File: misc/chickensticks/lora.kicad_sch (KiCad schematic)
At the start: 30 parts, among them J8 S02-25200300, J9 SMA, U4 LR2021IMLTRT, Y2 TG2520SMN 32.0000M-MCGNNM0

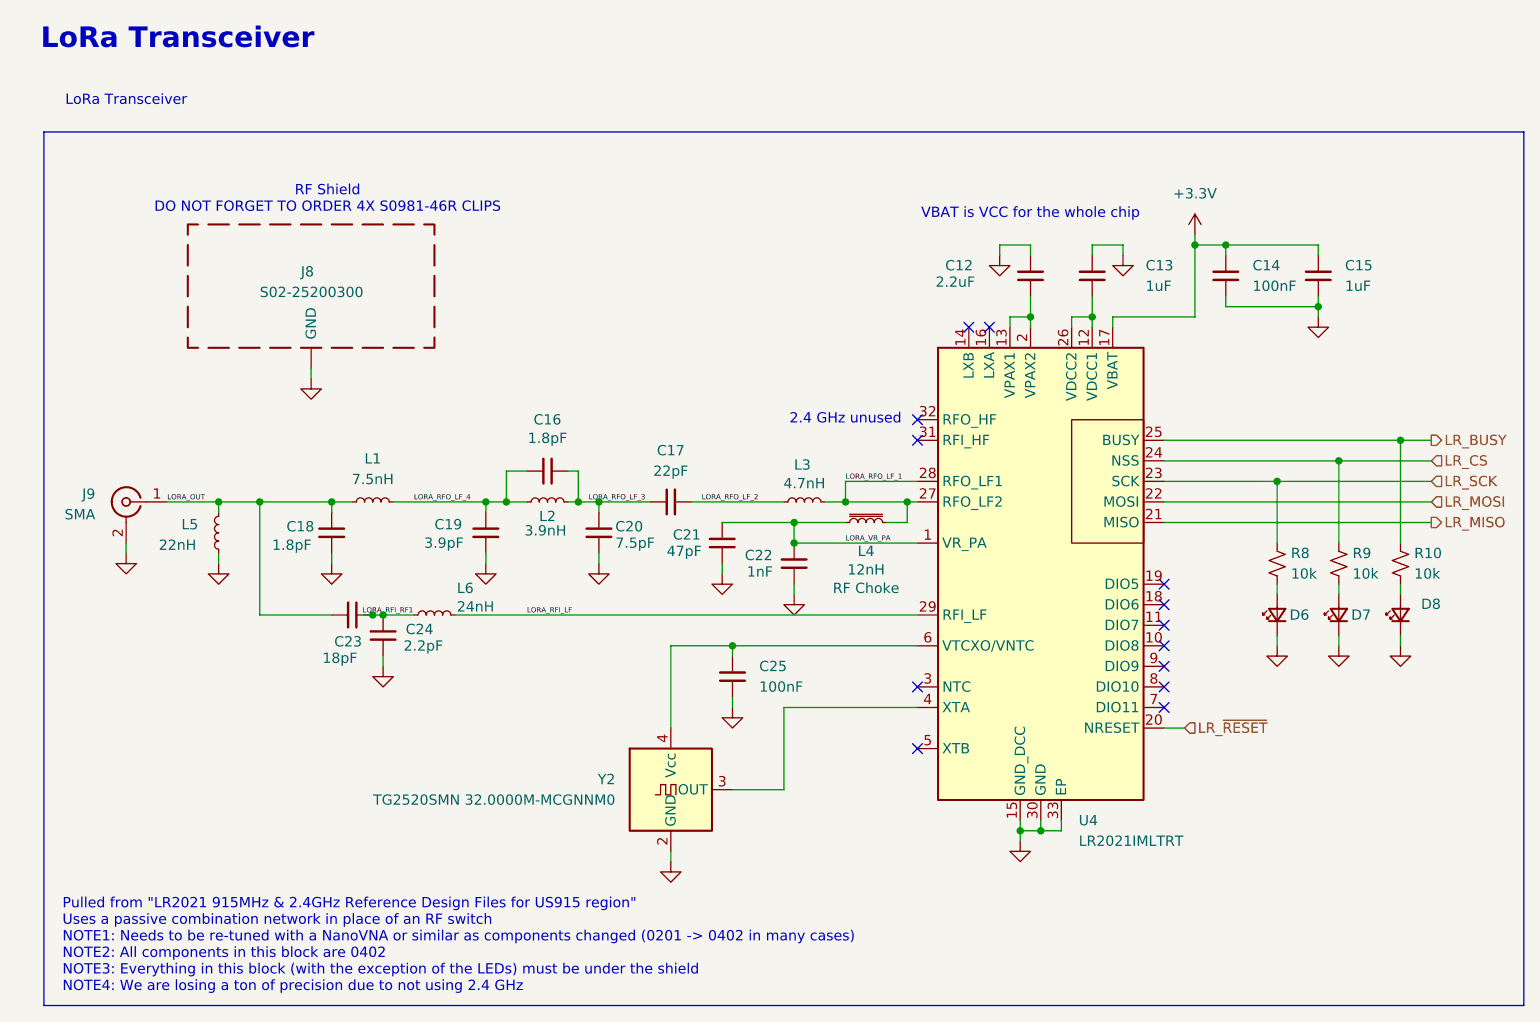
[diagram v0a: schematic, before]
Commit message: Simplify chickensticks, get isospi-tx ready, and update some cubemx projects
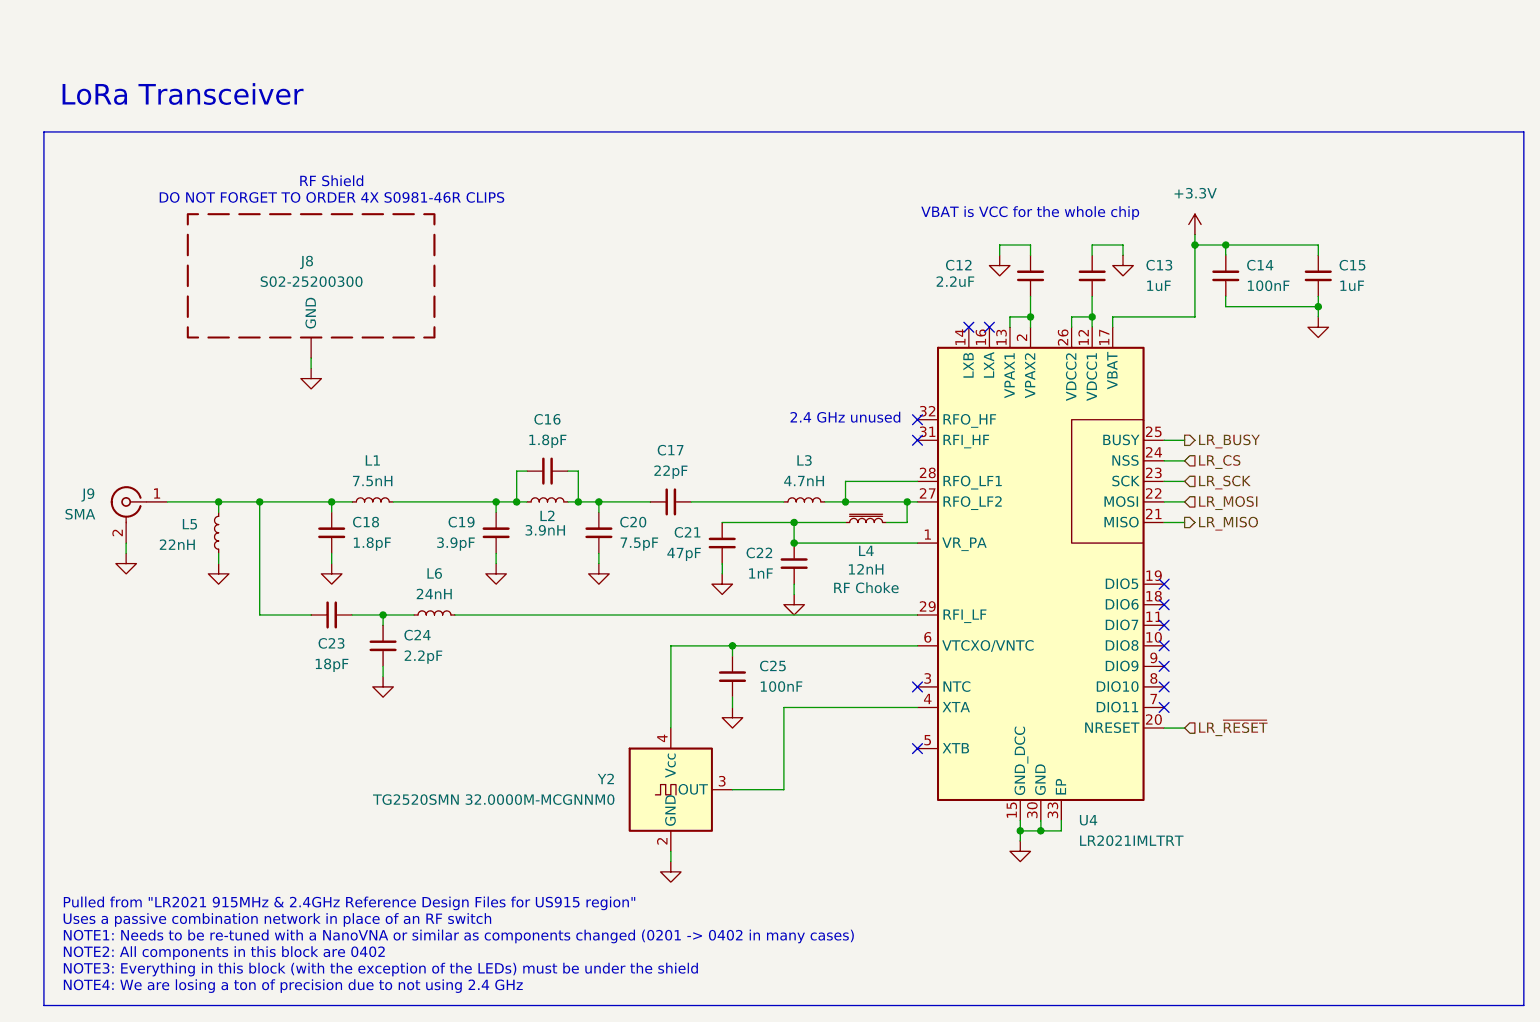
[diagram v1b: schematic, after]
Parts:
- removed D6, D7, D8: LED_Small, APRL_Passive:LED_0603, symbol Device:LED_Small
- removed R10, R8, R9: 10k, APRL_Passive:R_0603, symbol Device:R_Small_US
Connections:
- net LORA_OUT: no longer names the net of C18.2, C23.1, J9.1 (In), L1.1, L5.2
- net LORA_RFI_LF: no longer names the net of L6.2, U4.29 (RFI_LF)
- net LORA_RFI_RF1: no longer names the net of C23.2, C24.1, L6.1
- net LORA_RFO_LF_1: no longer names the net of L3.2, L4.2, U4.27 (RFO_LF2), U4.28 (RFO_LF1)
- net LORA_RFO_LF_2: no longer names the net of C17.1, L3.1
- net LORA_RFO_LF_3: no longer names the net of C16.1, C17.2, C20.2, L2.2
- net LORA_RFO_LF_4: no longer names the net of C16.2, C19.2, L1.2, L2.1
- net LORA_VR_PA: no longer names the net of C21.2, C22.2, L4.1, U4.1 (VR_PA)
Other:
- company: Aggie Propulsion & Rocketry Lab -> (none)
- title: Chickenstick -> (none)
- moved on the sheet: C19, C21, C22, C23, C24, J8
